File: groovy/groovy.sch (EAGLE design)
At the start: 6 parts, among them J1 USB_MICRO, U1 AP7312-1833

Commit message: add charger
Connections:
- new net N$1: C1.2, U1.VIN
- net VCC: no longer C1.2, U1.VIN
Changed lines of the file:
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@@
 <?xml version="1.0" encoding="utf-8"?>
 <!DOCTYPE eagle SYSTEM "eagle.dtd">
-<eagle version="9.1.3">
+<eagle version="9.0.1">
 <drawing>
 <settings>
@@
 <setting verticaltext="up"/>
 </settings>
-<grid distance="0.1" unitdist="inch" unit="inch" style="lines" multiple="1" display="no" altdistance="0.01" altunitdist="inch" altunit="inch"/>
+<grid distance="0.1" unitdist="inch" unit="inch" style="dots" multiple="1" display="yes" altdistance="0.01" altunitdist="inch" altunit="inch"/>
 <layers>
 <layer number="1" name="Top" color="4" fill="1" visible="no" active="no"/>
@@
 <part name="J1" library="scono" deviceset="USB_MICRO" device=""/>
 <part name="SUPPLY4" library="scono" deviceset="GND" device=""/>
-<part name="SUPPLY5" library="scono" deviceset="VCC" device=""/>
 <part name="SUPPLY6" library="scono" deviceset="GND" device=""/>
 <part name="U1" library="scono" deviceset="AP7312-1833" device=""/>
@@
 <instance part="J1" gate="G$1" x="22.86" y="139.7"/>
 <instance part="SUPPLY4" gate="GND" x="38.1" y="132.08"/>
-<instance part="SUPPLY5" gate="G$1" x="66.04" y="147.32"/>
 <instance part="SUPPLY6" gate="GND" x="119.38" y="157.48"/>
 <instance part="U1" gate="G$1" x="83.82" y="142.24"/>
@@
 <wire x1="33.02" y1="144.78" x2="38.1" y2="144.78" width="0.1524" layer="91"/>
 </segment>
-<segment>
-<pinref part="SUPPLY5" gate="G$1" pin="VCC"/>
-<pinref part="U1" gate="G$1" pin="VIN"/>
-<wire x1="66.04" y1="147.32" x2="73.66" y2="147.32" width="0.1524" layer="91"/>
-<pinref part="C1" gate="G$1" pin="2"/>
-<wire x1="66.04" y1="144.78" x2="66.04" y2="147.32" width="0.1524" layer="91"/>
-</segment>
 </net>
 <net name="GND" class="0">
@@
 </segment>
 </net>
+<net name="N$1" class="0">
+<segment>
+<pinref part="U1" gate="G$1" pin="VIN"/>
+<wire x1="66.04" y1="147.32" x2="73.66" y2="147.32" width="0.1524" layer="91"/>
+<pinref part="C1" gate="G$1" pin="2"/>
+<wire x1="66.04" y1="147.32" x2="66.04" y2="144.78" width="0.1524" layer="91"/>
+</segment>
+</net>

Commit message: remove old stuff, make some progress on power
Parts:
- added D1: RED, scono:LED0603
- added D2: GREEN, scono:LED0603
- added J2: 2_PIN_JST-XH, scono:2_PIN_JST-XH
- added J3: BL, scono:CONN_03
- added J4: PWR, scono:CONN_03
- added J5: UART, scono:CONN_02
- added R1, R2: 330, scono:R-US_R0603
- added R3: 5.1k, scono:R-US_R0603
- added U2: AP7312-1833, scono:AP7312-1833
- U1: value AP7312-1833 -> MCP73831T; device scono:AP7312-1833 -> scono:MCP73831T
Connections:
- new net MISO: J3.2
- new net MOSI: J3.1
- new net N$2: D2.A, R2.1
- new net N$4: R1.2, R2.2, U1.STAT
- new net N$5: R3.1, U1.PROG
- new net RX: J5.1
- new net SCK: J3.3
- new net TX: J5.2
- new net VBAT: C2.2, C3.2, J2.2, J4.3, U1.VBAT, U2.EN1, U2.EN2, U2.VIN
- net 1.8V: now also U2.VO2; no longer C3.2, U1.VO1
- net 3.3V: now also J4.1, U2.VO1; no longer C2.2, U1.EN1, U1.EN2, U1.VO2
- net GND: now also D2.C, J2.1, J4.2, R3.2, U2.GND
- net N$1: now also D1.C, R1.1; no longer C1.2, U1.VIN
- net VCC: now also C1.2, D1.A, U1.VDD

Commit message: do more audio stuff
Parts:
- added C10: 1uF, scono:CAP0603-CAP
- added C11, C15, C19: 10uF, scono:CAP0402-CAP
- added C12, C13, C14, C16, C17, C18, C20, C21, C22: 0.1uF, scono:CAP0402-CAP
- added C4: (no value), scono:CAP0603-CAP
- added C5, C6: 18pF, scono:CAP0603-CAP
- added C7, C8: 10nF, scono:CAP0603-CAP
- added C9: 47nF, scono:CAP0603-CAP
- added FB2: (no value), scono:FERRITE
- added R10, R4: 100K, scono:R-US_R0603
- added R11: 1M, scono:R-US_R0603
- added R5: 10R, scono:R-US_R0603
- added R6, R7: >VALUE, scono:R-US_R0603
- added R8, R9: 20R, scono:R-US_R0603
- added U3: VS1053, scono:VS1053
- added U4: ATMEGA328PB-AUR, scono:ATMEGA328PB-AUR
- added Y1: ABM8G-12.288MHZ-18-D2Y-T, scono:ABM8G-12.288MHZ-18-D2Y-T
- R1, R2: value 330 -> 330R
- R3: value 5.1k -> 10k
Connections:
- new net AVDD: C11.2, C12.2, C13.2, C14.2, FB2.P$1, U3.AVDD
- new net DREG: U3.DREQ
- new net GBUF: R5.1, U3.GBUF
- new net LEFT: R9.1, U3.LEFT
- new net N$23: U3.VCO
- new net N$24: C9.2, R5.2
- new net N$25: C8.1, R9.2
- new net N$27: R10.1, U3.GPIO0, U3.GPIO1, U3.GPIO2, U3.GPIO3, U3.GPIO4, U3.GPIO5, U3.GPIO6, U3.GPIO7
- new net N$3: C7.2, R8.2
- new net N$7: C4.2, R4.2, U3.!RESET!
- new net RCAP: C10.2, U3.RCAP
- new net RIGHT: R8.1, U3.RIGHT
- new net SCLK: U3.SCLK
- new net VSCS: U3.!CS!
- new net VSDCS: U3.!DCS!
- new net XTALIN: C5.1, R11.2, U3.XTALIN, Y1.3
- new net XTALOUT: C6.1, R11.1, U3.XTALOUT, Y1.1
- net 1.8V: now also C19.2, C20.2, C21.2, C22.2, U3.CVDD
- net 3.3V: now also C15.2, C16.2, C17.2, C18.2, FB2.P$2, R4.1, U3.IOVDD, U3.RX, U3.XTEST, U4.VCC
- net AGND: now also C10.1, C11.1, C12.1, C13.1, C14.1, C7.1, C8.2, C9.1, U3.AGND
- net GND: now also C15.1, C16.1, C17.1, C18.1, C19.1, C20.1, C21.1, C22.1, C4.1, C5.2, C6.2, R10.2, U3.DGND, Y1.GND
- net MISO: now also U3.MISO
- net MOSI: now also U3.MOSI
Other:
- moved on the sheet: C1, C2, C3

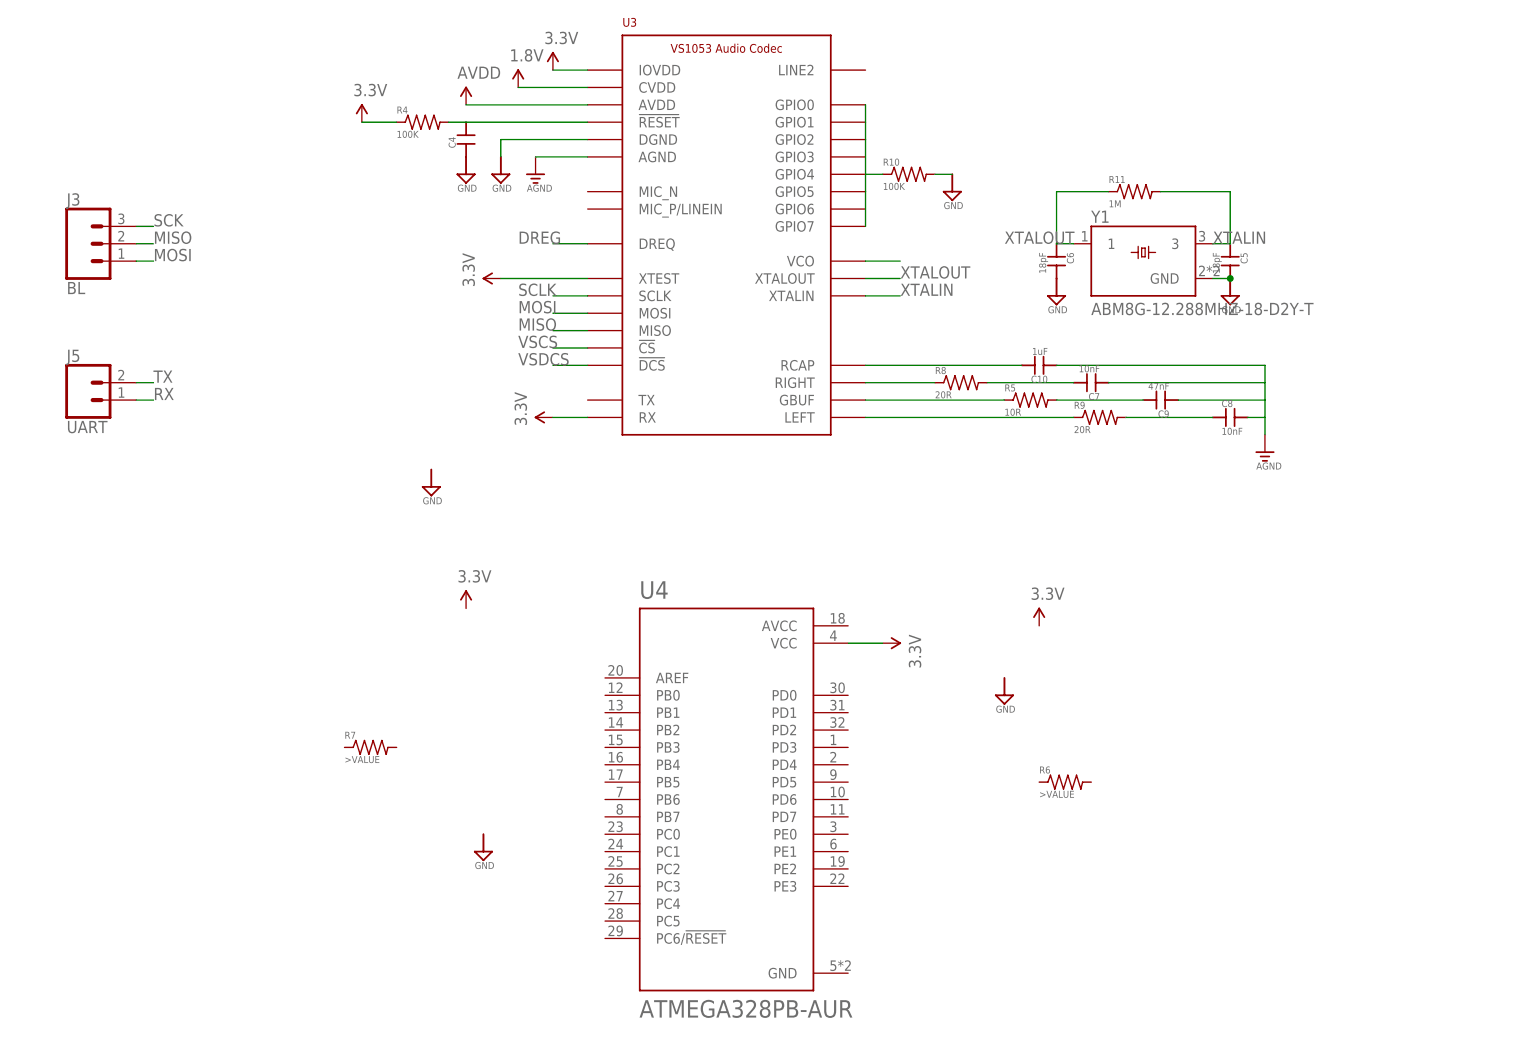
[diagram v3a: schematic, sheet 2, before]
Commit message: do more work on schem - need to add microphone
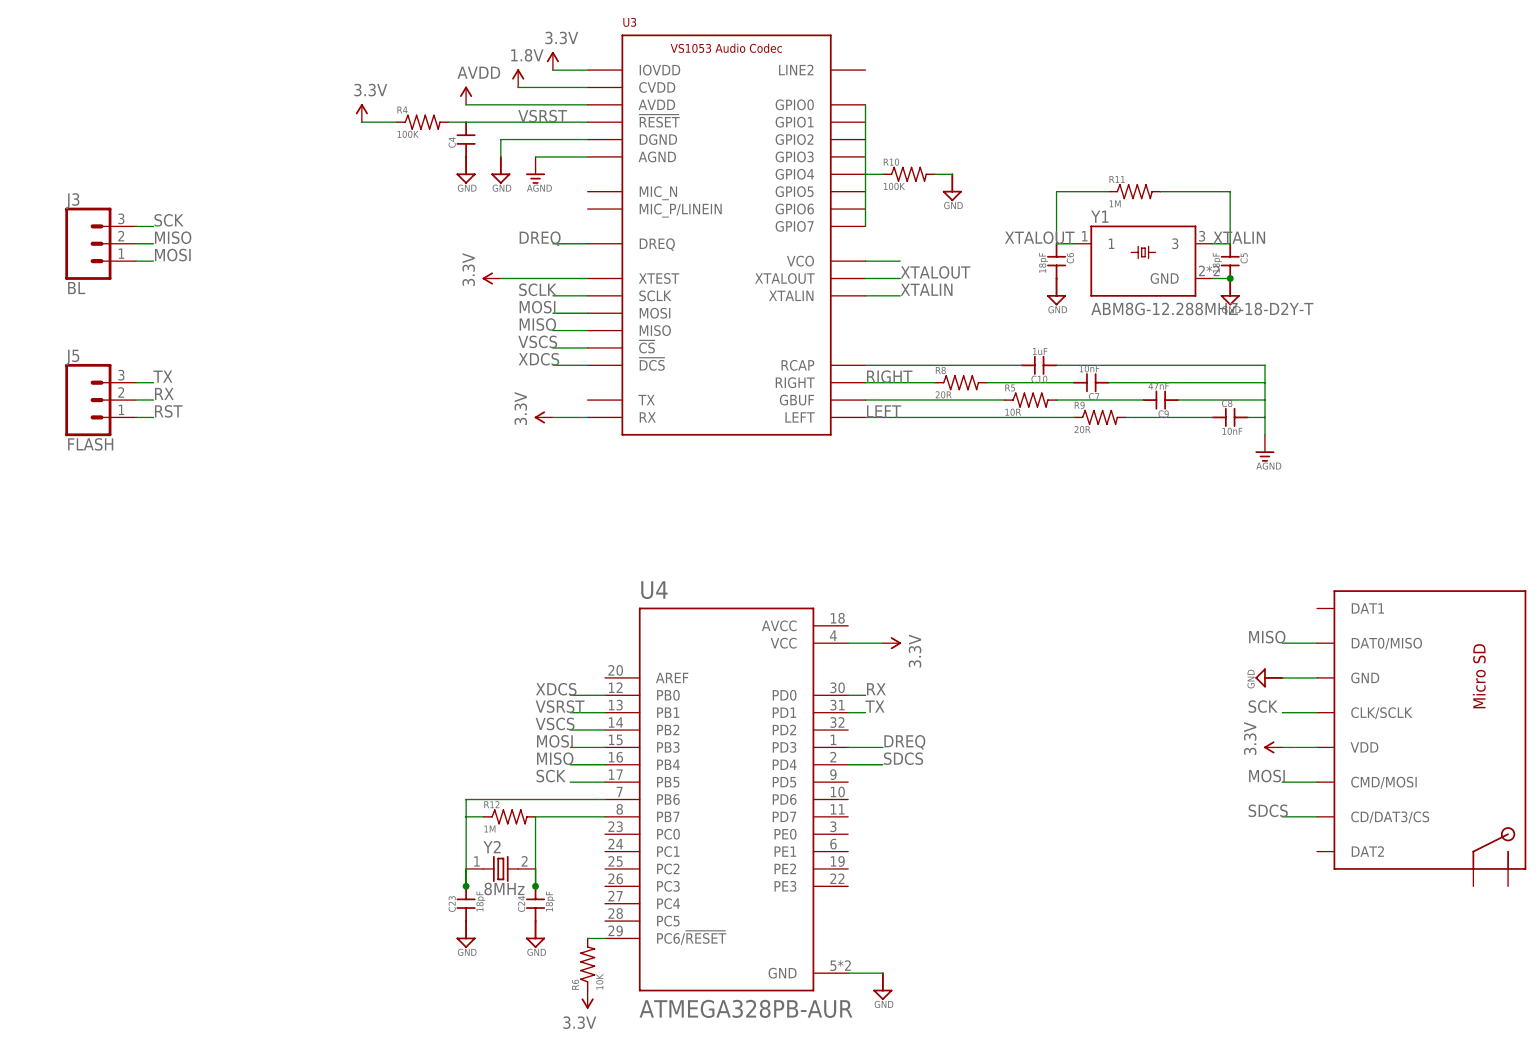
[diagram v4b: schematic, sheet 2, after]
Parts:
- removed R7: >VALUE, scono:R-US_R0603
- added C23, C24: 18pF, scono:CAP0603-CAP
- added P1: MICROSD, scono:MICROSD
- added R12: 1M, scono:R-US_R0603
- added Y2: 8MHz, scono:ABM3-8.000MHZ-D2Y-T
- J5: value UART -> FLASH; device scono:CONN_02 -> scono:CONN_03
- R6: value >VALUE -> 10K
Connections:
- removed net DREG: U3.DREQ
- removed net N$7: C4.2, R4.2, U3.!RESET!
- removed net VSDCS: U3.!DCS!
- new net DREQ: U3.DREQ, U4.PD3
- new net N$6: C23.2, R12.1, U4.PB6, Y2.1
- new net N$8: C24.2, R12.2, U4.PB7, Y2.2
- new net RST: J5.1, R6.2, U4.PC6/!RESET
- new net SDCS: P1.CD/DAT3/CS, U4.PD4
- new net VSRST: C4.2, R4.2, U3.!RESET!, U4.PB1
- new net XDCS: U3.!DCS!, U4.PB0
- net 3.3V: now also P1.VDD, R6.1
- net GND: now also C23.1, C24.1, P1.GND, U4.GND
- net MISO: now also P1.DAT0/MISO, U4.PB4
- net MOSI: now also P1.CMD/MOSI, U4.PB3
- net RX: now also J5.2, U4.PD0; no longer J5.1
- net SCK: now also P1.CLK/SCLK, U4.PB5
- net TX: now also J5.3, U4.PD1; no longer J5.2
- net VSCS: now also U4.PB2
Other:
- moved on the sheet: R6

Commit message: left over commit
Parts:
- added J6: SJ-3524-SMT, scono:SJ-3524-SMT
- added R13, R14, R7: 100k, scono:R-US_R0603
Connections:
- new net N$10: J6.4
- new net N$11: R14.2, U4.PD5
- new net N$7: R7.2, U4.PD7
- new net N$9: R13.2, U4.PD6
- net GND: now also J6.1, R13.1, R14.1, R7.1
- net LEFT: now also J6.2
- net RIGHT: now also J6.3
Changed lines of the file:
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@@
 <part name="SUPPLY15" library="scono" deviceset="GND" device=""/>
 <part name="U$5" library="scono" deviceset="3.3V" device=""/>
+<part name="J6" library="scono" deviceset="SJ-3524-SMT" device=""/>
+<part name="SUPPLY18" library="scono" deviceset="GND" device=""/>
+<part name="R7" library="scono" deviceset="R-US_" device="R0603" value="100k"/>
+<part name="R13" library="scono" deviceset="R-US_" device="R0603" value="100k"/>
+<part name="R14" library="scono" deviceset="R-US_" device="R0603" value="100k"/>
+<part name="SUPPLY27" library="scono" deviceset="GND" device=""/>
+<part name="SUPPLY28" library="scono" deviceset="GND" device=""/>
+<part name="SUPPLY29" library="scono" deviceset="GND" device=""/>
 </parts>
 <sheets>
@@
 <instance part="SUPPLY15" gate="GND" x="200.66" y="81.28" rot="R270"/>
 <instance part="U$5" gate="G$1" x="203.2" y="71.12" rot="R90"/>
+<instance part="J6" gate="G$1" x="25.4" y="71.12"/>
+<instance part="SUPPLY18" gate="GND" x="45.72" y="76.2" rot="R90"/>
+<instance part="R7" gate="G$1" x="162.56" y="55.88" rot="R90"/>
+<instance part="R13" gate="G$1" x="167.64" y="55.88" rot="R90"/>
+<instance part="R14" gate="G$1" x="172.72" y="55.88" rot="R90"/>
+<instance part="SUPPLY27" gate="GND" x="162.56" y="48.26"/>
+<instance part="SUPPLY28" gate="GND" x="167.64" y="48.26"/>
+<instance part="SUPPLY29" gate="GND" x="172.72" y="48.26"/>
 </instances>
 <busses>
@@
 <label x="142.24" y="119.38" size="1.778" layer="95"/>
 </segment>
+<segment>
+<pinref part="J6" gate="G$1" pin="2"/>
+<wire x1="38.1" y1="68.58" x2="43.18" y2="68.58" width="0.1524" layer="91"/>
+<label x="48.26" y="68.58" size="1.778" layer="95" rot="R180"/>
+</segment>
 </net>
 <net name="GBUF" class="0">
@@
 <wire x1="142.24" y1="124.46" x2="152.4" y2="124.46" width="0.1524" layer="91"/>
 <label x="142.24" y="124.46" size="1.778" layer="95"/>
+</segment>
+<segment>
+<pinref part="J6" gate="G$1" pin="3"/>
+<wire x1="38.1" y1="73.66" x2="43.18" y2="73.66" width="0.1524" layer="91"/>
+<label x="48.26" y="73.66" size="1.778" layer="95" rot="R180"/>
 </segment>
 </net>
@@
 <pinref part="SUPPLY15" gate="GND" pin="GND"/>
 </segment>
+<segment>
+<pinref part="J6" gate="G$1" pin="1"/>
+<wire x1="38.1" y1="76.2" x2="43.18" y2="76.2" width="0.1524" layer="91"/>
+<pinref part="SUPPLY18" gate="GND" pin="GND"/>
+</segment>
+<segment>
+<pinref part="R7" gate="G$1" pin="1"/>
+<pinref part="SUPPLY27" gate="GND" pin="GND"/>
+</segment>
+<segment>
+<pinref part="R13" gate="G$1" pin="1"/>
+<pinref part="SUPPLY28" gate="GND" pin="GND"/>
+</segment>
+<segment>
+<pinref part="R14" gate="G$1" pin="1"/>
+<pinref part="SUPPLY29" gate="GND" pin="GND"/>
+</segment>
 </net>
 <net name="XTALIN" class="0">
@@
 </segment>
 </net>
+<net name="N$10" class="0">
+<segment>
+<pinref part="J6" gate="G$1" pin="4"/>
+<wire x1="38.1" y1="71.12" x2="43.18" y2="71.12" width="0.1524" layer="91"/>
+</segment>
+</net>
+<net name="N$7" class="0">
+<segment>
+<pinref part="U4" gate="G$1" pin="PD7"/>
+<wire x1="139.7" y1="60.96" x2="162.56" y2="60.96" width="0.1524" layer="91"/>
+<pinref part="R7" gate="G$1" pin="2"/>
+<wire x1="162.56" y1="60.96" x2="162.56" y2="58.42" width="0.1524" layer="91"/>
+<wire x1="162.56" y1="60.96" x2="177.8" y2="60.96" width="0.1524" layer="91"/>
+</segment>
+</net>
+<net name="N$9" class="0">
+<segment>
+<pinref part="U4" gate="G$1" pin="PD6"/>
+<wire x1="139.7" y1="63.5" x2="167.64" y2="63.5" width="0.1524" layer="91"/>
+<pinref part="R13" gate="G$1" pin="2"/>
+<wire x1="167.64" y1="63.5" x2="167.64" y2="58.42" width="0.1524" layer="91"/>
+<wire x1="167.64" y1="63.5" x2="177.8" y2="63.5" width="0.1524" layer="91"/>
+</segment>
+</net>
+<net name="N$11" class="0">
+<segment>
+<pinref part="U4" gate="G$1" pin="PD5"/>
+<wire x1="139.7" y1="66.04" x2="172.72" y2="66.04" width="0.1524" layer="91"/>
+<pinref part="R14" gate="G$1" pin="2"/>
+<wire x1="172.72" y1="66.04" x2="172.72" y2="58.42" width="0.1524" layer="91"/>
+<wire x1="172.72" y1="66.04" x2="177.8" y2="66.04" width="0.1524" layer="91"/>
+</segment>
+</net>
